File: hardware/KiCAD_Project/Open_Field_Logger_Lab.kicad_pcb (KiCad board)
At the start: 4 copper layers, 107.9 x 69.8 mm, 62 parts, among them J1 1-0001899, J10 1-0001899, J11 1-0001899, J12 1-0001899, J13 1-0001899, J14 1-0001899, J2 1-0001894, J3 1-0001894, J4 AUX Input, J5 NP_Conn_01x03, J6 NP_Conn_01x06, J7 NP_Conn_01x04, J8 1-0000127, J9 Conn_01x01, Q1 1-0000163, Q2 1-0000163, Q3 1-0000163, SW1 1-0000681, U1 1-0001893, U2 1-0001890, U3 1-0001892, U4 1-0001891, Y1 1-0001901

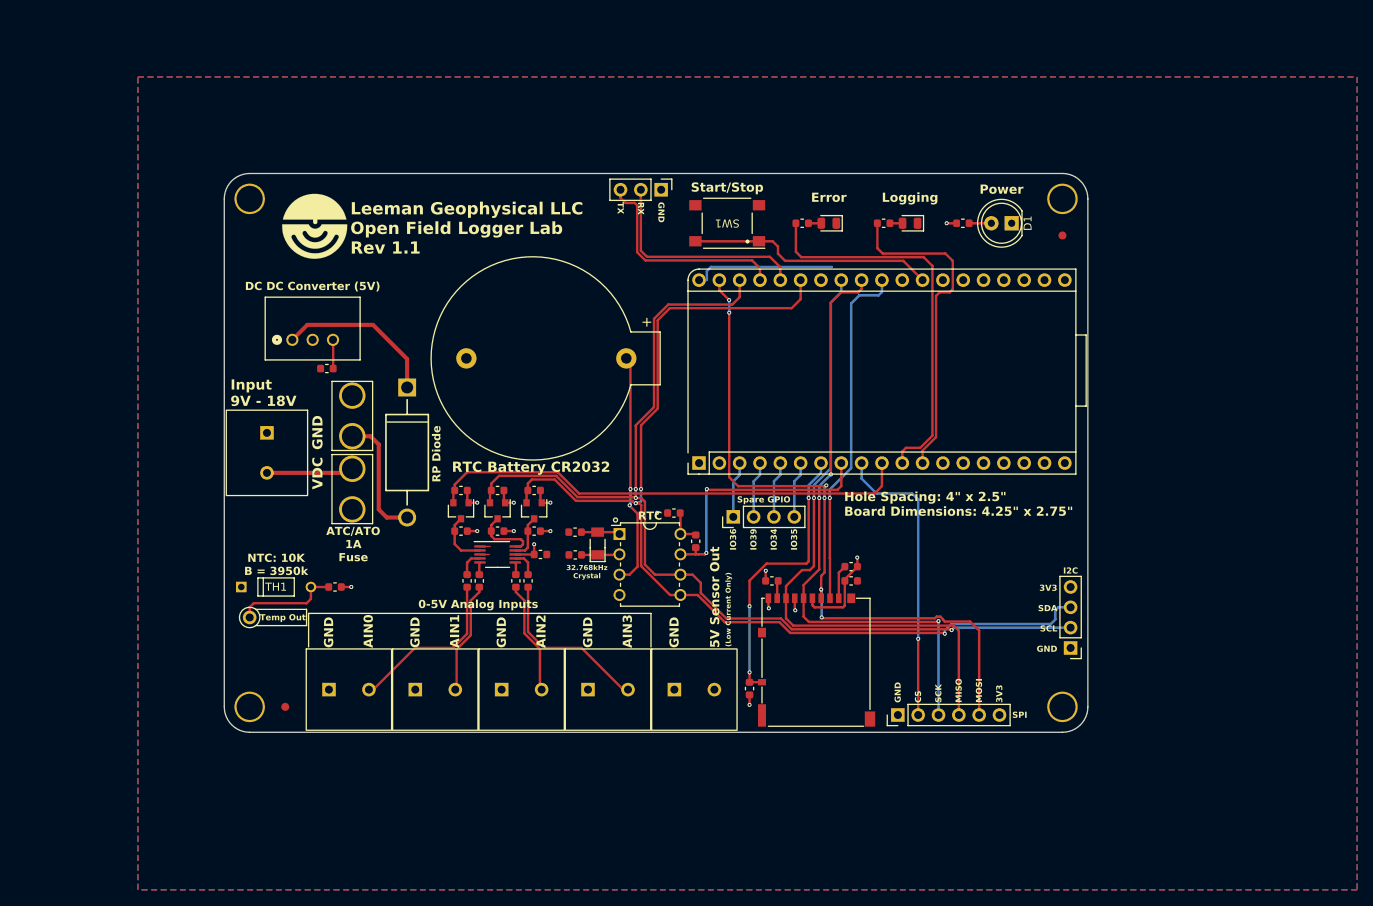
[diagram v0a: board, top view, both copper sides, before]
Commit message: Rev 1.2 Redesign: Major Changes: - Switch to SMD ESP32-S3 with updated GPIO mapping - Added 3.3V regulation and USB-C Powering - Added dual-source power support - Replaced RTC battery with 1F supercap - Replaced microSD with SPI Flash - Updated supporting circuitry
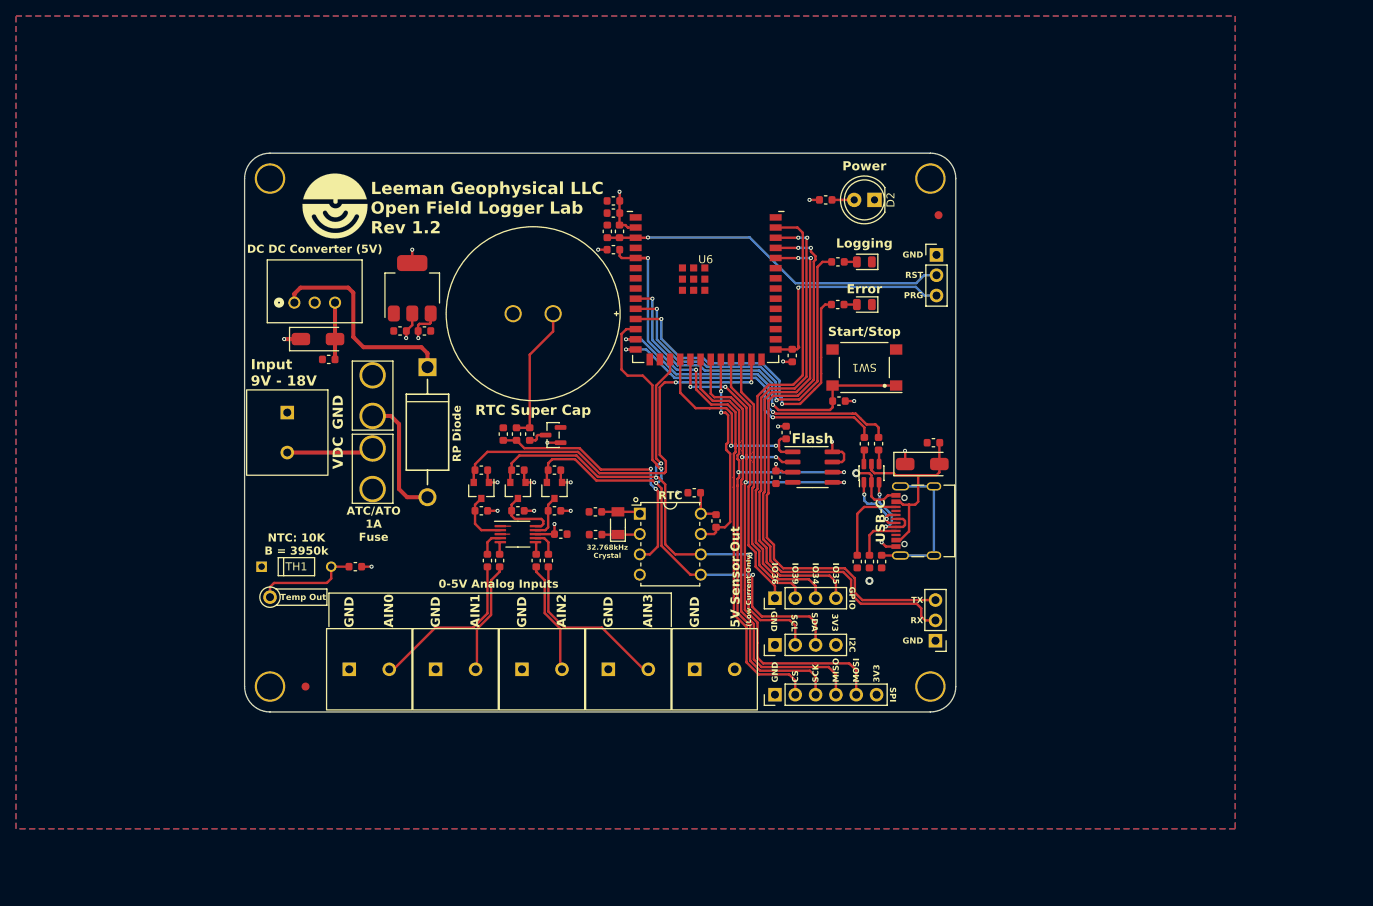
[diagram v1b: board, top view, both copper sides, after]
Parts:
- removed BT1: 1-0000863, batteries:1-0000863
- removed the C5 at (171.7, 113.8)
- removed the J8 at (161.4, 116.0)
- removed the R11 at (159.0, 127.3)
- removed the R12 at (161.8, 113.8)
- removed the R13 at (171.7, 112.0)
- removed the U2 at (175.6, 87.6)
- added C1: 1-0001956, capacitors_th:1-0001956, F.Cu at (132.0, 80.4)
- added C10: 1-0000007, capacitors_0603:1-0000007, F.Cu at (162.3, 100.8)
- added C11: 1-0000018, capacitors_0603:1-0000018, F.Cu at (141.2, 70.1)
- added C12: 1-0000015, capacitors_0603:1-0000015, F.Cu at (142.0, 66.3)
- added C13: 1-0000007, capacitors_0603:1-0000007, F.Cu at (142.0, 67.8)
- added C14: 1-0000018, capacitors_0603:1-0000018, F.Cu at (182.0, 96.5)
- added C2: 1-0000904, capacitors_0603:1-0000904, F.Cu at (128.2, 95.4)
- added C8: 1-0000018, capacitors_0603:1-0000018, F.Cu at (118.4, 82.5)
- added C9: 1-0000324, capacitors_0603:1-0000324, F.Cu at (115.3, 82.5)
- added D1: 1-0001955, diodes:1-0001955, F.Cu at (134.4, 95.6)
- added D6: 1-0001977, diodes:1-0001977, F.Cu at (105.1, 83.6)
- added D7: 1-0001931, diodes:1-0001931, F.Cu at (174.2, 100.3)
- added D8: 1-0001977, diodes:1-0001977, F.Cu at (180.6, 99.2)
- added J15: 1-0001974, connectors:1-0001974, F.Cu at (181.0, 106.3)
- added J9: NP_Conn_01x03, np_connectors:PinHeader_1x03_P2.54mm_Vertical, F.Cu at (182.4, 73.0)
- added R16: 1-0000010, resistors_0603:1-0000010, F.Cu at (142.7, 70.1)
- added R18: 1-0001933, resistors_0603:1-0001933, F.Cu at (173.4, 96.6)
- added R19: 1-0001933, resistors_0603:1-0001933, F.Cu at (175.1, 96.6)
- added R20: 1-0001859, resistors_0603:1-0001859, F.Cu at (174.0, 111.4)
- added R21: 1-0001859, resistors_0603:1-0001859, F.Cu at (172.5, 111.4)
- added R22: 1-0000006, resistors_0603:1-0000006, F.Cu at (175.5, 111.4)
- added R23: 1-0000010, resistors_0603:1-0000010, F.Cu at (163.6, 95.2)
- added R24: 1-0000010, resistors_0603:1-0000010, F.Cu at (142.0, 72.4)
- added R26: 1-0000010, resistors_0603:1-0000010, F.Cu at (170.2, 91.3)
- added R27: 1-0000010, resistors_0603:1-0000010, F.Cu at (164.3, 85.6)
- added R4: 1-0000112, resistors_0603:1-0000112, F.Cu at (131.5, 95.4)
- added R9: 1-0000013, resistors_0603:1-0000013, F.Cu at (129.9, 95.4)
- added U4: 1-0001973, regulators:1-0001973, F.Cu at (116.8, 77.2)
- added U5: 1-0001976, eeproms:1-0001976, F.Cu at (166.9, 99.6)
- added U6: 1-0001927, microcontrollers:1-0001927, F.Cu at (153.5, 73.6)
- moved J10 66.0 mm to (182.2, 121.3), turned to 180 degrees
- moved J12 37.0 mm to (162.2, 121.8), turned to 90 degrees
- moved SW1 24.9 mm to (173.4, 87.1)
- moved D2 17.4 mm to (174.6, 66.2)
- moved R1 17.4 mm to (168.5, 66.2)
- moved H3 16.7 mm to (181.6, 63.5)
- moved H1 16.7 mm to (181.6, 127.0)
- moved FID2 15.7 mm to (182.6, 68.1)
- moved J11 15.6 mm to (162.2, 128.0)
- moved J13 11.4 mm to (162.2, 116.0)
- moved D4 11.1 mm to (173.4, 79.2)
- moved R3 11.1 mm to (170.0, 79.2)
- moved D3 7.48 mm to (173.4, 73.9)
- moved R2 7.48 mm to (170.1, 73.9)
- moved U3 4.66 mm to (107.2, 79.0)
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- renumbered C6 to C3, C2 to C4, C3 to C5, C4 to C6, C1 to C7, D1 to D2, D2 to D3, D3 to D5, J5 to J10, J6 to J11, J7 to J12, J4 to J13, J9 to J14, J10 to J2, J11 to J3, J12 to J4, J13 to J5, J14 to J6, J2 to J7, J3 to J8, R8 to R10, R9 to R11, R10 to R12, R5 to R13, R6 to R14, R7 to R15, R14 to R17, R3 to R25, R4 to R3, R15 to R5, R16 to R6, R17 to R7, R18 to R8, U4 to U1, U3 to U2, U1 to U3
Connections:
- net Net-(U1-Vin) renamed VDC
- C7 pad 1: +5V -> Net-(D6-A)
- U3 pad 3: +5V -> Net-(D6-A)
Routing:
- net Net-(J13-Pin_4): track 7.06 -> 60.9 mm, vias 0 -> 2
- net I2C_SDA: track 130.9 -> 78.3 mm
- net Net-(J13-Pin_3): track 7.06 -> 58.9 mm
- net I2C_SCL: track 126.1 -> 74.4 mm
- net RX: track 27.5 -> 72.3 mm, vias 0 -> 2
- net TX: track 27.0 -> 71.6 mm, vias 0 -> 2
- net Reset_CTRL: track 0.00 -> 43.9 mm, vias 0 -> 1
- net SD_CS: track 43.9 -> 0.00 mm, vias 1 -> 0
- net USB_D-: track 0.00 -> 40.2 mm, vias 0 -> 2
- net USB_D+: track 0.00 -> 38.0 mm, vias 0 -> 2
- net EXT_CS: track 37.0 -> 73.2 mm, vias 1 -> 2
- net SD_CD: track 35.6 -> 0.00 mm, vias 3 -> 0
- net Program_CTRL: track 0.00 -> 28.3 mm, vias 0 -> 1
- net Net-(J13-Pin_2): track 7.06 -> 33.8 mm
- net MEM_CS: track 0.00 -> 25.7 mm, vias 0 -> 2
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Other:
- board size 107.9 x 69.8 mm -> 88.9 x 69.9 mm
- board text added: "3-0000321"
- board text added: "Flash"
- board text added: "GPIO"
- board text added: "Leeman Geophysical LLC Open Field Logger Lab Rev 1.2"
- board text added: "PRG"
- board text added: "RST"
- board text added: "RTC Super Cap"
- board text added: "USB-C"
- board text removed: "3-0000307"
- board text removed: "Hole Spacing: 4{dblquote} x 2.5{dblquote} Board Dimensions: 4.25{dblquote} x 2.75{dblquote}"
- board text removed: "Leeman Geophysical LLC Open Field Logger Lab Rev 1.1"
- board text removed: "RTC Battery CR2032"
- board text removed: "Spare GPIO"
